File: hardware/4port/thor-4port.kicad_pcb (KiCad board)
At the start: 2 copper layers, 177 x 65 mm, 24 parts, among them J1 THOR J47 / Wieson, J10 AUX / RAW IO, J12 SHIELD / GND / OPEN, J2 FSI_CAN0 / CAN, J3 FSI_CAN1 / CAN, J4 AURIX_CAN1 / CAN, J5 AURIX_CAN2 / CAN

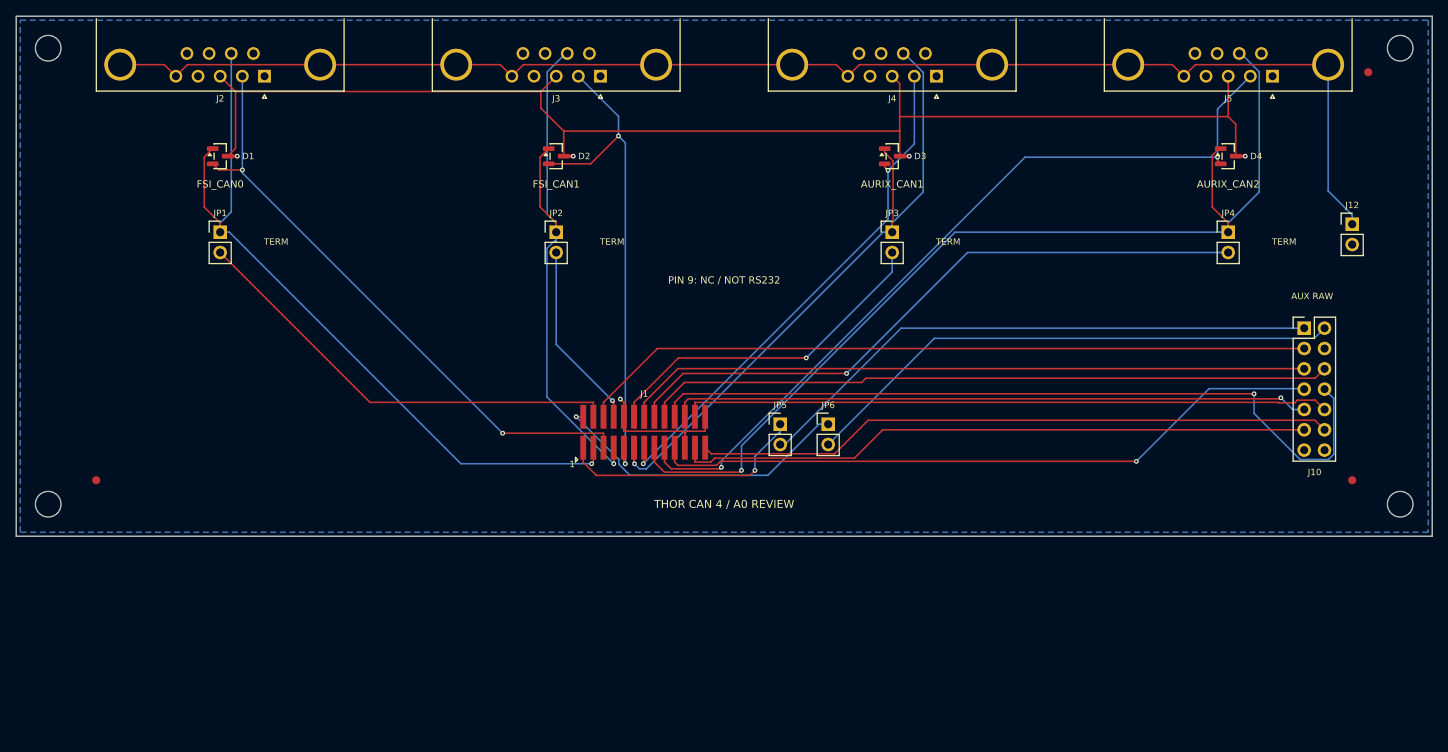
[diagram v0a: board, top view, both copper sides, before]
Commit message: Revise A1 CAN routing, enclosure identity and engineering documentation
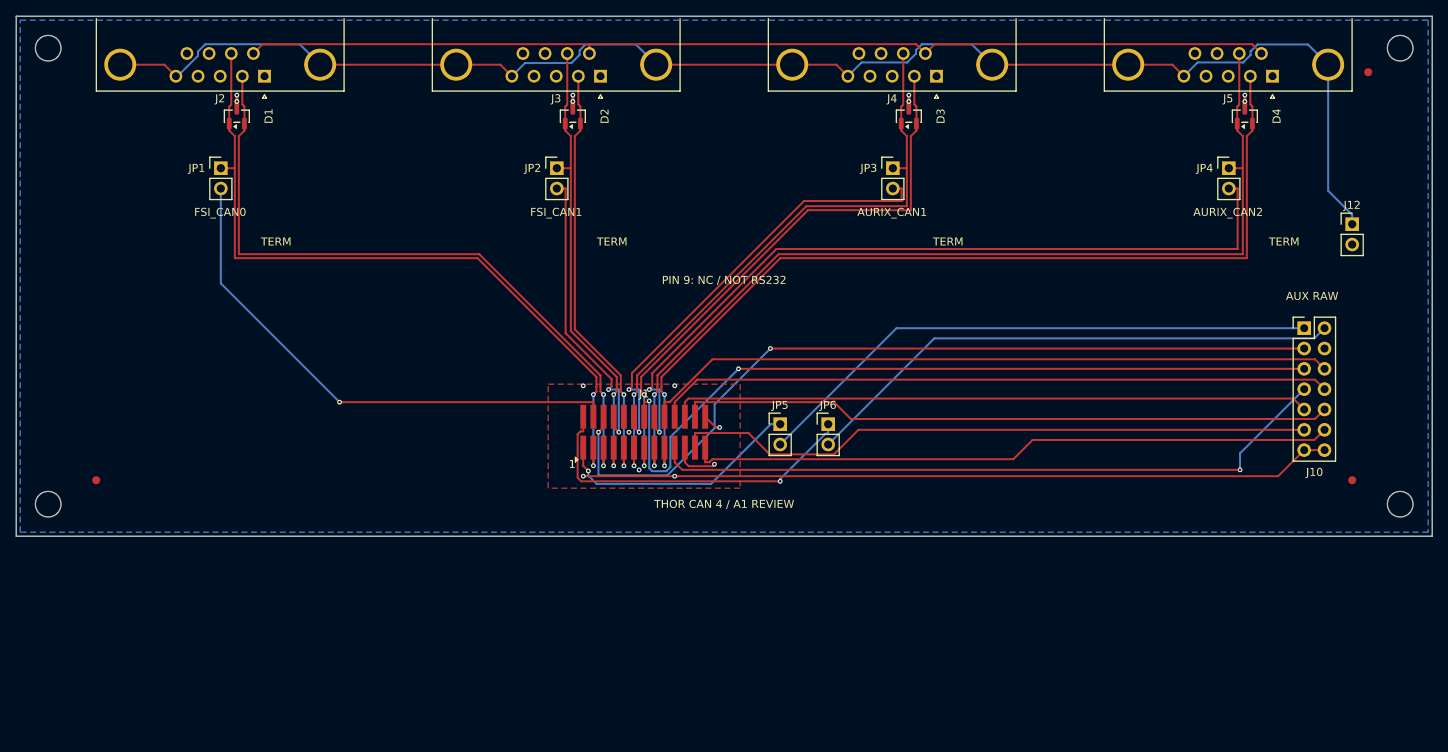
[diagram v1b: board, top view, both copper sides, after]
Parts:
- moved JP1 8.00 mm to (25.6, 19.0)
- moved JP2 8.00 mm to (67.6, 19.0)
- moved JP3 8.00 mm to (109.6, 19.0)
- moved JP4 8.00 mm to (151.6, 19.0)
- moved D4 5.42 mm to (153.6, 12.5), turned to 90 degrees
- moved D1 5.42 mm to (27.6, 12.5), turned to 90 degrees
- moved D2 5.42 mm to (69.6, 12.5), turned to 90 degrees
- moved D3 5.42 mm to (111.6, 12.5), turned to 90 degrees
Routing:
- net /GND: track 188.2 -> 241.7 mm, vias 5 -> 16
- net /AURIX_CAN2_TERM: track 81.3 -> 99.3 mm, vias 1 -> 2
- net /AURIX_CAN2_L: track 100.7 -> 116.0 mm
- net /ESTOP_IN1: track 86.1 -> 100.5 mm, vias 0 -> 2
- net /FSI_CAN1_TERM: track 23.5 -> 37.6 mm, vias 1 -> 2
- net /AURIX_PWM_GPIO: track 98.4 -> 84.7 mm, vias 1 -> 0
- net /AURIX_CAN1_TERM: track 43.3 -> 56.3 mm, vias 1 -> 2
- net /FSI_CAN1_H: track 70.8 -> 58.5 mm, vias 1 -> 2
- net /FSI_EXT_GPIO1: track 92.2 -> 104.1 mm, vias 0 -> 2
- net /FSI_CAN0_L: track 76.5 -> 87.9 mm
- net /FSI_CAN0_TERM: track 56.2 -> 66.4 mm, vias 0 -> 1
- net /SHIELD: track 176.9 -> 186.5 mm
- net /FSI_CAN1_L: track 63.1 -> 53.9 mm
- net /AURIX_CAN1_L: track 65.5 -> 73.0 mm
- net /AURIX_CAN1_H: track 82.8 -> 77.4 mm, vias 1 -> 2
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- added copper zone on F.Cu, net /GND
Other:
- board text added: "THOR CAN 4 / A1 REVIEW"
- board text removed: "THOR CAN 4 / A0 REVIEW"

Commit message: Add prototype access, clear controls and reinforced mounting housings
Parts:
- added P1: ISOLATED PROTOTYPING PADS, Thor:Prototype_23x6_P2.54, F.Cu at (10.0, 72.0)
- added P2: ISOLATED PROTOTYPING PADS, Thor:Prototype_31x6_P2.54, F.Cu at (90.5, 72.0)
- added TP1: PROTO POWER / JP5-JP6 GATED, Thor:Prototype_Power_3x3_P2.54, F.Cu at (10.0, 62.0)
- added TP2: PROTO POWER / JP5-JP6 GATED, Thor:Prototype_Power_3x3_P2.54, F.Cu at (90.5, 62.0)
- moved H3 25.0 mm to (4.00, 86.0)
- moved H4 25.0 mm to (173.0, 86.0)
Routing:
- net /AUX_5V_AO: track 68.1 -> 170.8 mm
- net /AUX_3V3: track 71.5 -> 168.4 mm
- net /GND: track 241.7 -> 255.1 mm
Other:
- board size 177 x 65 mm -> 177 x 90 mm
- board text added: "10"
- board text added: "11"
- board text added: "12"
- board text added: "13"
- board text added: "14"
- board text added: "15"
- board text added: "16"
- board text added: "17"
- board text added: "18"
- board text added: "19"
- board text added: "2"
- board text added: "20"
- board text added: "21"
- board text added: "22"
- board text added: "23"
- board text added: "24"
- board text added: "25"
- board text added: "26"
- board text added: "27"
- board text added: "28"
- board text added: "29"
- board text added: "3"
- board text added: "30"
- board text added: "31"
- board text added: "3V3"
- board text added: "4"
- board text added: "5"
- board text added: "5V"
- board text added: "6"
- board text added: "7"
- board text added: "8"
- board text added: "9"
- board text added: "A"
- board text added: "A1 DEV"
- board text added: "AUX: SHUNT = ON"
- board text added: "B"
- board text added: "C"
- board text added: "CAN0"
- board text added: "CAN0 TERM"
- board text added: "CAN1"
- board text added: "CAN1 TERM"
- board text added: "D"
- board text added: "DEFAULT OPEN"
- board text added: "E"
- board text added: "F"
- board text added: "FSI6"
- board text added: "FSI6: FSI FIRMWARE / NOT LINUX GPIO"
- board text added: "GND"
- board text added: "J10 RAW I/O"
- board text added: "JP1 = 120R"
- board text added: "JP2 = 120R"
- board text added: "JP3 = 120R"
- board text added: "JP4 = 120R"
- board text added: "KEEP CLEAR"
- board text added: "OPEN"
- board text added: "OUT1"
- board text added: "P1 / ISOLATED 2.54"
- board text added: "P2 / ISOLATED 2.54"
- board text added: "PGOOD"
- board text added: "PIN 9 NC / CAN ONLY"
- board text added: "PWM"
- board text added: "RES2"
- board text added: "RES2 TERM"
- board text added: "RES3"
- board text added: "RES3 TERM"
- board text added: "RIBBON"
- board text added: "SCL"
- board text added: "SDA"
- board text added: "SHIELD"
- board text added: "STOP1"
- board text added: "STOP2"
- board text added: "THOR CAN"
- board text added: "WAKE"
- board text added: "github.com/mvalancy"
- board text removed: "AURIX_CAN1"
- board text removed: "AURIX_CAN2"
- board text removed: "AUX RAW"
- board text removed: "FSI_CAN0"
- board text removed: "FSI_CAN1"
- board text removed: "PIN 9: NC / NOT RS232"
- board text removed: "TERM"
- board text removed: "THOR CAN 4 / A1 REVIEW"
